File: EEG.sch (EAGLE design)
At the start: 0 parts

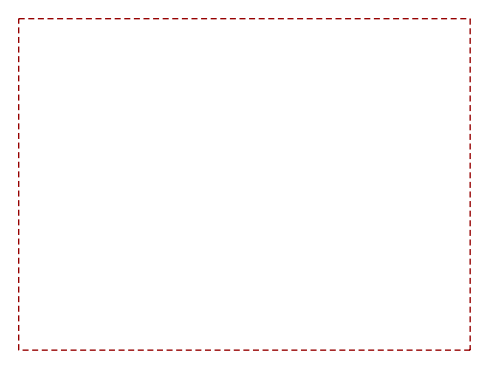
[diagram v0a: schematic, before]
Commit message: INA medio agregado
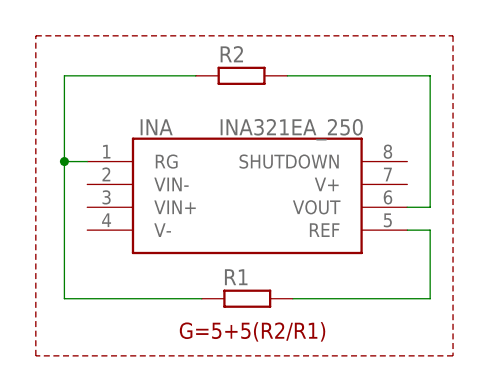
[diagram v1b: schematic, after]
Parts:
- added INA: INA321EA_250, INA321EA_250:INA321EA_250
- added R1, R2: (no value), rcl:R-EU_R0805
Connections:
- new net N$1: INA.RG, R1.1, R2.1
- new net N$2: INA.REF, R1.2
- new net N$4: INA.VOUT, R2.2
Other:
- note added: "G=5+5(R2/R1)"
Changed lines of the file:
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@@
 <parts>
 <part name="FRAME1" library="frames" library_urn="urn:adsk.eagle:library:229" deviceset="LETTER_L" device=""/>
+<part name="INA" library="INA321EA_250" deviceset="INA321EA_250" device=""/>
+<part name="R1" library="rcl" library_urn="urn:adsk.eagle:library:334" deviceset="R-EU_" device="R0805" package3d_urn="urn:adsk.eagle:package:23553/2"/>
+<part name="R2" library="rcl" library_urn="urn:adsk.eagle:library:334" deviceset="R-EU_" device="R0805" package3d_urn="urn:adsk.eagle:package:23553/2"/>
 </parts>
 <sheets>
 <sheet>
 <plain>
-<wire x1="17.78" y1="170.815" x2="67.945" y2="170.815" width="0.1524" layer="94" style="shortdash"/>
-<wire x1="67.945" y1="170.815" x2="67.945" y2="133.985" width="0.1524" layer="94" style="shortdash"/>
-<wire x1="67.945" y1="133.985" x2="17.78" y2="133.985" width="0.1524" layer="94" style="shortdash"/>
-<wire x1="17.78" y1="133.985" x2="17.78" y2="170.815" width="0.1524" layer="94" style="shortdash"/>
+<wire x1="19.685" y1="168.91" x2="66.04" y2="168.91" width="0.1524" layer="94" style="shortdash"/>
+<wire x1="66.04" y1="168.91" x2="66.04" y2="133.35" width="0.1524" layer="94" style="shortdash"/>
+<wire x1="66.04" y1="133.35" x2="19.685" y2="133.35" width="0.1524" layer="94" style="shortdash"/>
+<wire x1="19.685" y1="133.35" x2="19.685" y2="168.91" width="0.1524" layer="94" style="shortdash"/>
+<text x="35.56" y="135.255" size="1.778" layer="94">G=5+5(R2/R1)</text>
 </plain>
 <instances>
@@
 <attribute name="DRAWING_NAME" x="165.1" y="19.05" size="2.54" layer="94"/>
 </instance>
+<instance part="INA" gate="G$1" x="25.4" y="154.94" smashed="yes">
+<attribute name="NAME" x="31.115" y="158.75" size="1.778" layer="95" align="center-left"/>
+<attribute name="VALUE" x="40.005" y="158.75" size="1.778" layer="96" align="center-left"/>
+</instance>
+<instance part="R1" gate="G$1" x="43.18" y="139.7" smashed="yes">
+<attribute name="NAME" x="40.48125" y="141.1986" size="1.778" layer="95"/>
+<attribute name="VALUE" x="39.37" y="136.398" size="1.778" layer="96"/>
+</instance>
+<instance part="R2" gate="G$1" x="42.545" y="164.465" smashed="yes">
+<attribute name="NAME" x="40.005" y="165.9636" size="1.778" layer="95"/>
+<attribute name="VALUE" x="38.735" y="161.163" size="1.778" layer="96"/>
+</instance>
 </instances>
 <busses>
 </busses>
 <nets>
+<net name="N$2" class="0">
+<segment>
+<pinref part="INA" gate="G$1" pin="REF"/>
+<wire x1="60.96" y1="147.32" x2="63.5" y2="147.32" width="0.1524" layer="91"/>
+<wire x1="63.5" y1="147.32" x2="63.5" y2="139.7" width="0.1524" layer="91"/>
+<pinref part="R1" gate="G$1" pin="2"/>
+<wire x1="63.5" y1="139.7" x2="48.26" y2="139.7" width="0.1524" layer="91"/>
+</segment>
+</net>
+<net name="N$4" class="0">
+<segment>
+<pinref part="INA" gate="G$1" pin="VOUT"/>
+<wire x1="60.96" y1="149.86" x2="63.5" y2="149.86" width="0.1524" layer="91"/>
+<pinref part="R2" gate="G$1" pin="2"/>
+<wire x1="63.5" y1="149.86" x2="63.5" y2="164.465" width="0.1524" layer="91"/>
+<wire x1="63.5" y1="164.465" x2="47.625" y2="164.465" width="0.1524" layer="91"/>
+</segment>
+</net>
+<net name="N$1" class="0">
+<segment>
+<pinref part="R1" gate="G$1" pin="1"/>
+<wire x1="38.1" y1="139.7" x2="22.86" y2="139.7" width="0.1524" layer="91"/>
+<pinref part="INA" gate="G$1" pin="RG"/>
+<wire x1="22.86" y1="139.7" x2="22.86" y2="154.94" width="0.1524" layer="91"/>
+<wire x1="22.86" y1="154.94" x2="25.4" y2="154.94" width="0.1524" layer="91"/>
+<pinref part="R2" gate="G$1" pin="1"/>
+<wire x1="37.465" y1="164.465" x2="22.86" y2="164.465" width="0.1524" layer="91"/>
+<wire x1="22.86" y1="164.465" x2="22.86" y2="154.94" width="0.1524" layer="91"/>
+<junction x="22.86" y="154.94"/>
+</segment>
+</net>
 </nets>
 </sheet>
@@
 will not be understood (or retained) with this version.
 </note>
+<note version="8.3" severity="warning">
+Since Version 8.3, EAGLE supports the association of 3D packages
+with devices in libraries, schematics, and board files. Those 3D
+packages will not be understood (or retained) with this version.
+</note>
+<note version="8.4" severity="warning">
+Since Version 8.4, EAGLE supports properties for SPICE simulation.
+Probes in schematics and SPICE mapping objects found in parts and library devices
+will not be understood with this version. Update EAGLE to the latest version
+for full support of SPICE simulation.
+</note>
 </compatibility>

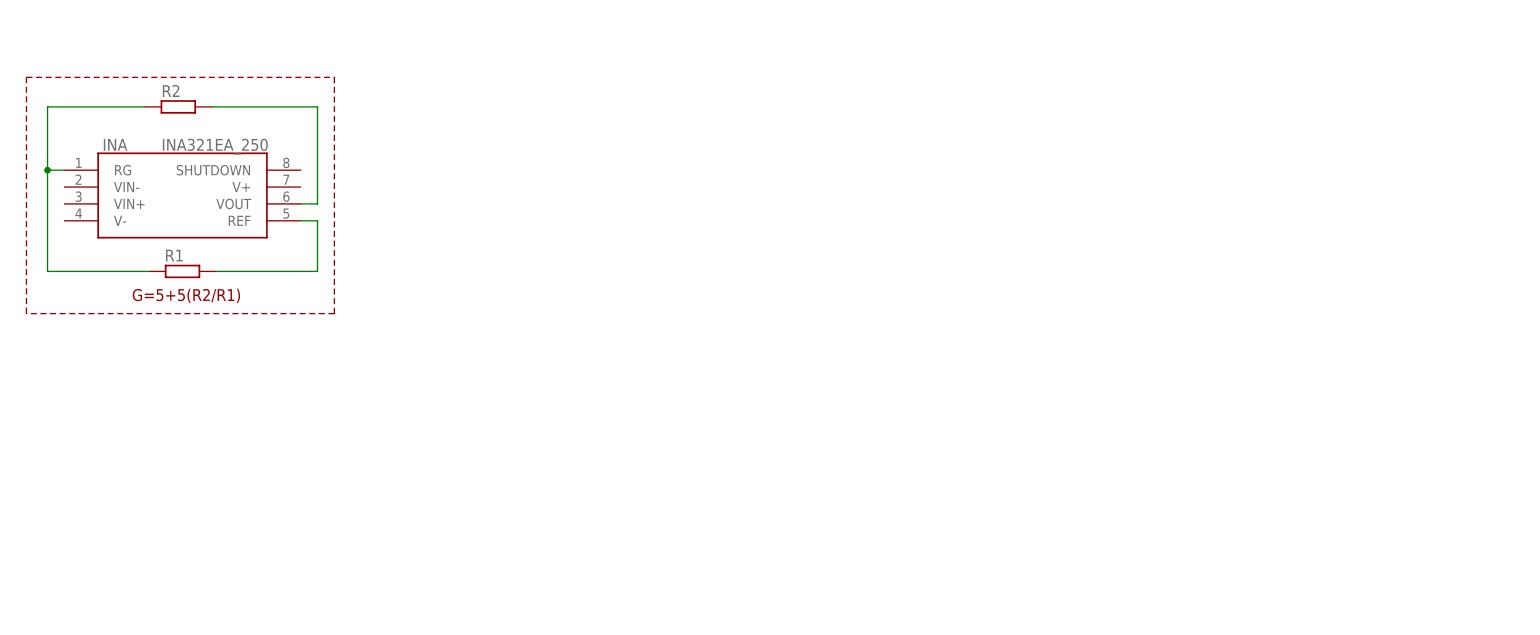
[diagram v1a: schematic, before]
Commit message: Se agregó la forma del filtro pasa banda
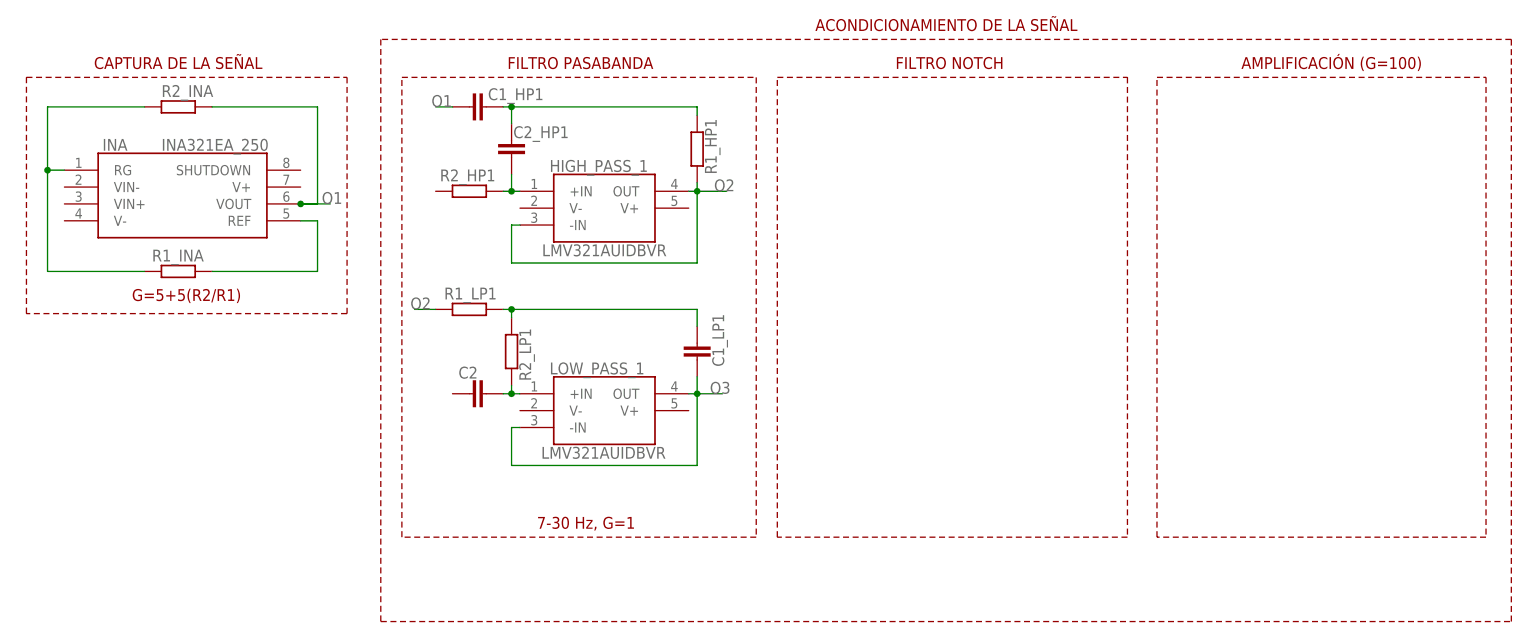
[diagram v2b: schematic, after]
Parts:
- removed R1: (no value), rcl:R-EU_R0805
- added C1_HP1, C1_LP1, C2, C2_HP1: (no value), rcl:C-EUC0805
- added HIGH_PASS_1, LOW_PASS_1: LMV321AUIDBVR, LMV321AUIDBVR:LMV321AUIDBVR
- added R1_HP1, R1_INA, R1_LP1, R2_HP1, R2_LP1: (no value), rcl:R-EU_R0805
- renumbered R2 to R2_INA
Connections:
- new net N$5: C2_HP1.2, HIGH_PASS_1.+IN, R2_HP1.2
- new net N$6: C1_HP1.2, C2_HP1.1, R1_HP1.2
- new net N$7: C2.1, LOW_PASS_1.+IN, R2_LP1.2
- new net O1: C1_HP1.1, INA.VOUT, R2_INA.2
- new net O2: HIGH_PASS_1.-IN, HIGH_PASS_1.OUT, R1_HP1.1, R1_LP1.1
- new net O3: C1_LP1.2, LOW_PASS_1.-IN, LOW_PASS_1.OUT
- net N$1: now also R1_INA.1; no longer R1.1
- net N$2: now also R1_INA.2; no longer R1.2
- net N$4: now also C1_LP1.1, R1_LP1.2, R2_LP1.1; no longer INA.VOUT, R2_INA.2
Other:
- note added: "7-30 Hz, G=1"
- note added: "ACONDICIONAMIENTO DE LA SEÑAL"
- note added: "AMPLIFICACIÓN (G=100)"
- note added: "CAPTURA DE LA SEÑAL"
- note added: "FILTRO NOTCH"
- note added: "FILTRO PASABANDA"

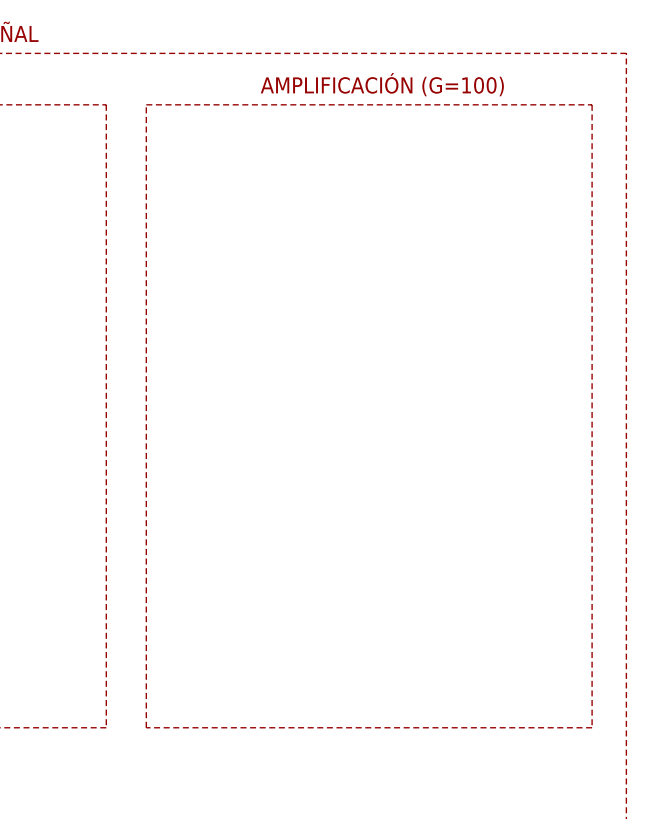
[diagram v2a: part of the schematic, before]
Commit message: Se añadió la forma del driver amplificador
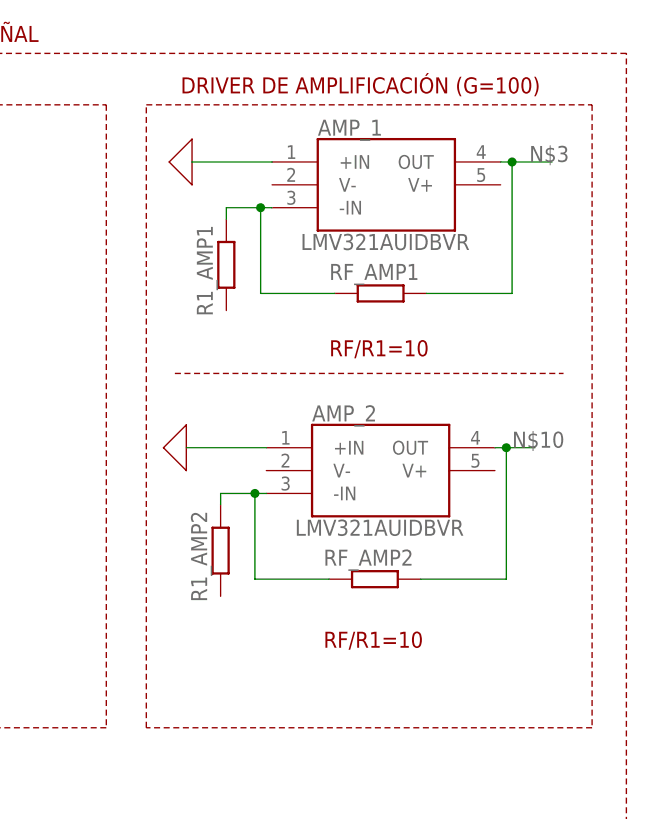
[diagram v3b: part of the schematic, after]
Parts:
- added AMP_1, AMP_2: LMV321AUIDBVR, LMV321AUIDBVR:LMV321AUIDBVR
- added R1_AMP1, R1_AMP2, RF_AMP1, RF_AMP2: (no value), rcl:R-EU_R0805
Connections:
- new net 0: AMP_1.+IN, AMP_2.+IN
- new net N$10: AMP_2.OUT, RF_AMP2.2
- new net N$3: AMP_1.OUT, RF_AMP1.2
- new net N$8: AMP_1.-IN, R1_AMP1.2, RF_AMP1.1
- new net N$9: AMP_2.-IN, R1_AMP2.2, RF_AMP2.1
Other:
- note added: "DRIVER DE AMPLIFICACIÓN (G=100)"
- note added: "RF/R1=10"
- note removed: "AMPLIFICACIÓN (G=100)"
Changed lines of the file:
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@@
 <layer number="97" name="Info" color="7" fill="1" visible="yes" active="yes"/>
 <layer number="98" name="Guide" color="6" fill="1" visible="yes" active="yes"/>
+<layer number="99" name="SpiceOrder" color="7" fill="1" visible="yes" active="yes"/>
 </layers>
 <schematic xreflabel="%F%N/%S.%C%R" xrefpart="/%S.%C%R">
@@
 <part name="R2_LP1" library="rcl" library_urn="urn:adsk.eagle:library:334" deviceset="R-EU_" device="R0805" package3d_urn="urn:adsk.eagle:package:23553/2"/>
 <part name="C2" library="rcl" library_urn="urn:adsk.eagle:library:334" deviceset="C-EU" device="C0805" package3d_urn="urn:adsk.eagle:package:23617/2"/>
+<part name="AMP_1" library="LMV321AUIDBVR" deviceset="LMV321AUIDBVR" device=""/>
+<part name="X_1" library="ngspice-simulation" library_urn="urn:adsk.eagle:library:527439" deviceset="GND" device=""/>
+<part name="RF_AMP1" library="rcl" library_urn="urn:adsk.eagle:library:334" deviceset="R-EU_" device="R0805" package3d_urn="urn:adsk.eagle:package:23553/2"/>
+<part name="R1_AMP1" library="rcl" library_urn="urn:adsk.eagle:library:334" deviceset="R-EU_" device="R0805" package3d_urn="urn:adsk.eagle:package:23553/2"/>
+<part name="AMP_2" library="LMV321AUIDBVR" deviceset="LMV321AUIDBVR" device=""/>
+<part name="X_2" library="ngspice-simulation" library_urn="urn:adsk.eagle:library:527439" deviceset="GND" device=""/>
+<part name="RF_AMP2" library="rcl" library_urn="urn:adsk.eagle:library:334" deviceset="R-EU_" device="R0805" package3d_urn="urn:adsk.eagle:package:23553/2"/>
+<part name="R1_AMP2" library="rcl" library_urn="urn:adsk.eagle:library:334" deviceset="R-EU_" device="R0805" package3d_urn="urn:adsk.eagle:package:23553/2"/>
 </parts>
 <sheets>
@@
 <text x="92.075" y="170.18" size="1.778" layer="94">FILTRO PASABANDA</text>
 <text x="150.495" y="170.18" size="1.778" layer="94">FILTRO NOTCH</text>
-<text x="202.565" y="170.18" size="1.778" layer="94">AMPLIFICACIÓN (G=100)</text>
+<text x="193.675" y="170.18" size="1.778" layer="94">DRIVER DE AMPLIFICACIÓN (G=100)</text>
 <wire x1="76.2" y1="168.91" x2="129.54" y2="168.91" width="0.1524" layer="94" style="shortdash"/>
 <wire x1="129.54" y1="168.91" x2="129.54" y2="99.695" width="0.1524" layer="94" style="shortdash"/>
@@
 <wire x1="189.865" y1="99.695" x2="189.865" y2="168.91" width="0.1524" layer="94" style="shortdash"/>
 <text x="96.52" y="100.965" size="1.778" layer="94">7-30 Hz, G=1</text>
+<text x="210.185" y="140.97" size="1.778" layer="94">RF/R1=10</text>
+<text x="209.55" y="108.585" size="1.778" layer="94">RF/R1=10</text>
+<wire x1="193.04" y1="139.065" x2="236.22" y2="139.065" width="0.1524" layer="94" style="dashdot"/>
 </plain>
 <instances>
@@
 <attribute name="NAME" x="84.709" y="123.571" size="1.778" layer="95"/>
 <attribute name="VALUE" x="84.201" y="119.761" size="1.778" layer="96" rot="R270"/>
+</instance>
+<instance part="AMP_1" gate="G$1" x="203.835" y="162.56" smashed="yes">
+<attribute name="NAME" x="208.915" y="166.37" size="1.778" layer="95" align="center-left"/>
+<attribute name="VALUE" x="207.01" y="153.67" size="1.778" layer="96" align="center-left"/>
+</instance>
+<instance part="X_1" gate="G$1" x="194.945" y="162.56" smashed="yes" rot="R270"/>
+<instance part="RF_AMP1" gate="G$1" x="215.9" y="147.955" smashed="yes">
+<attribute name="NAME" x="210.185" y="149.4536" size="1.778" layer="95"/>
+<attribute name="VALUE" x="212.09" y="144.653" size="1.778" layer="96"/>
+</instance>
+<instance part="R1_AMP1" gate="G$1" x="198.755" y="151.13" smashed="yes" rot="R90">
+<attribute name="NAME" x="197.2564" y="145.415" size="1.778" layer="95" rot="R90"/>
+<attribute name="VALUE" x="202.057" y="147.32" size="1.778" layer="96" rot="R90"/>
+</instance>
+<instance part="AMP_2" gate="G$1" x="203.2" y="130.81" smashed="yes">
+<attribute name="NAME" x="208.28" y="134.62" size="1.778" layer="95" align="center-left"/>
+<attribute name="VALUE" x="206.375" y="121.92" size="1.778" layer="96" align="center-left"/>
+</instance>
+<instance part="X_2" gate="G$1" x="194.31" y="130.81" smashed="yes" rot="R270"/>
+<instance part="RF_AMP2" gate="G$1" x="215.265" y="116.205" smashed="yes">
+<attribute name="NAME" x="209.55" y="117.7036" size="1.778" layer="95"/>
+<attribute name="VALUE" x="211.455" y="112.903" size="1.778" layer="96"/>
+</instance>
+<instance part="R1_AMP2" gate="G$1" x="198.12" y="119.38" smashed="yes" rot="R90">
+<attribute name="NAME" x="196.6214" y="113.665" size="1.778" layer="95" rot="R90"/>
+<attribute name="VALUE" x="201.422" y="115.57" size="1.778" layer="96" rot="R90"/>
 </instance>
 </instances>
@@
 </segment>
 </net>
+<net name="N$3" class="0">
+<segment>
+<pinref part="AMP_1" gate="G$1" pin="OUT"/>
+<wire x1="229.235" y1="162.56" x2="230.505" y2="162.56" width="0.1524" layer="91"/>
+<label x="232.41" y="162.56" size="1.778" layer="95"/>
+<pinref part="RF_AMP1" gate="G$1" pin="2"/>
+<wire x1="230.505" y1="162.56" x2="234.95" y2="162.56" width="0.1524" layer="91"/>
+<wire x1="220.98" y1="147.955" x2="230.505" y2="147.955" width="0.1524" layer="91"/>
+<wire x1="230.505" y1="147.955" x2="230.505" y2="162.56" width="0.1524" layer="91"/>
+<junction x="230.505" y="162.56"/>
+</segment>
+</net>
+<net name="0" class="0">
+<segment>
+<pinref part="AMP_1" gate="G$1" pin="+IN"/>
+<pinref part="X_1" gate="G$1" pin="0"/>
+<wire x1="203.835" y1="162.56" x2="194.945" y2="162.56" width="0.1524" layer="91"/>
+</segment>
+<segment>
+<pinref part="AMP_2" gate="G$1" pin="+IN"/>
+<pinref part="X_2" gate="G$1" pin="0"/>
+<wire x1="203.2" y1="130.81" x2="194.31" y2="130.81" width="0.1524" layer="91"/>
+</segment>
+</net>
+<net name="N$8" class="0">
+<segment>
+<pinref part="RF_AMP1" gate="G$1" pin="1"/>
+<wire x1="210.82" y1="147.955" x2="202.565" y2="147.955" width="0.1524" layer="91"/>
+<wire x1="202.565" y1="147.955" x2="202.565" y2="157.48" width="0.1524" layer="91"/>
+<pinref part="AMP_1" gate="G$1" pin="-IN"/>
+<wire x1="202.565" y1="157.48" x2="203.835" y2="157.48" width="0.1524" layer="91"/>
+<pinref part="R1_AMP1" gate="G$1" pin="2"/>
+<wire x1="198.755" y1="156.21" x2="198.755" y2="157.48" width="0.1524" layer="91"/>
+<wire x1="198.755" y1="157.48" x2="202.565" y2="157.48" width="0.1524" layer="91"/>
+<junction x="202.565" y="157.48"/>
+</segment>
+</net>
+<net name="N$9" class="0">
+<segment>
+<pinref part="AMP_2" gate="G$1" pin="-IN"/>
+<wire x1="203.2" y1="125.73" x2="201.93" y2="125.73" width="0.1524" layer="91"/>
+<pinref part="R1_AMP2" gate="G$1" pin="2"/>
+<wire x1="201.93" y1="125.73" x2="198.12" y2="125.73" width="0.1524" layer="91"/>
+<wire x1="198.12" y1="125.73" x2="198.12" y2="124.46" width="0.1524" layer="91"/>
+<pinref part="RF_AMP2" gate="G$1" pin="1"/>
+<wire x1="210.185" y1="116.205" x2="201.93" y2="116.205" width="0.1524" layer="91"/>
+<wire x1="201.93" y1="116.205" x2="201.93" y2="125.73" width="0.1524" layer="91"/>
+<junction x="201.93" y="125.73"/>
+</segment>
+</net>
+<net name="N$10" class="0">
+<segment>
+<pinref part="RF_AMP2" gate="G$1" pin="2"/>
+<wire x1="220.345" y1="116.205" x2="229.87" y2="116.205" width="0.1524" layer="91"/>
+<wire x1="229.87" y1="116.205" x2="229.87" y2="130.81" width="0.1524" layer="91"/>
+<pinref part="AMP_2" gate="G$1" pin="OUT"/>
+<wire x1="229.87" y1="130.81" x2="228.6" y2="130.81" width="0.1524" layer="91"/>
+<wire x1="229.87" y1="130.81" x2="233.045" y2="130.81" width="0.1524" layer="91"/>
+<junction x="229.87" y="130.81"/>
+<label x="230.505" y="130.81" size="1.778" layer="95"/>
+</segment>
+</net>
